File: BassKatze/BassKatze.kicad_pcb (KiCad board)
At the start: 2 copper layers, 55 x 54.9 mm, 54 parts, among them J1 Conn_01x02_Female, Q1 IRF7404, Q2 BSS138, Q3 BSS138, Q4 BSS138, Q5 BSS138, Q6 BSS138, SW1 SW_Push, U1 ATmega328-AU, U2 MSGEQ7, U3 TP4056

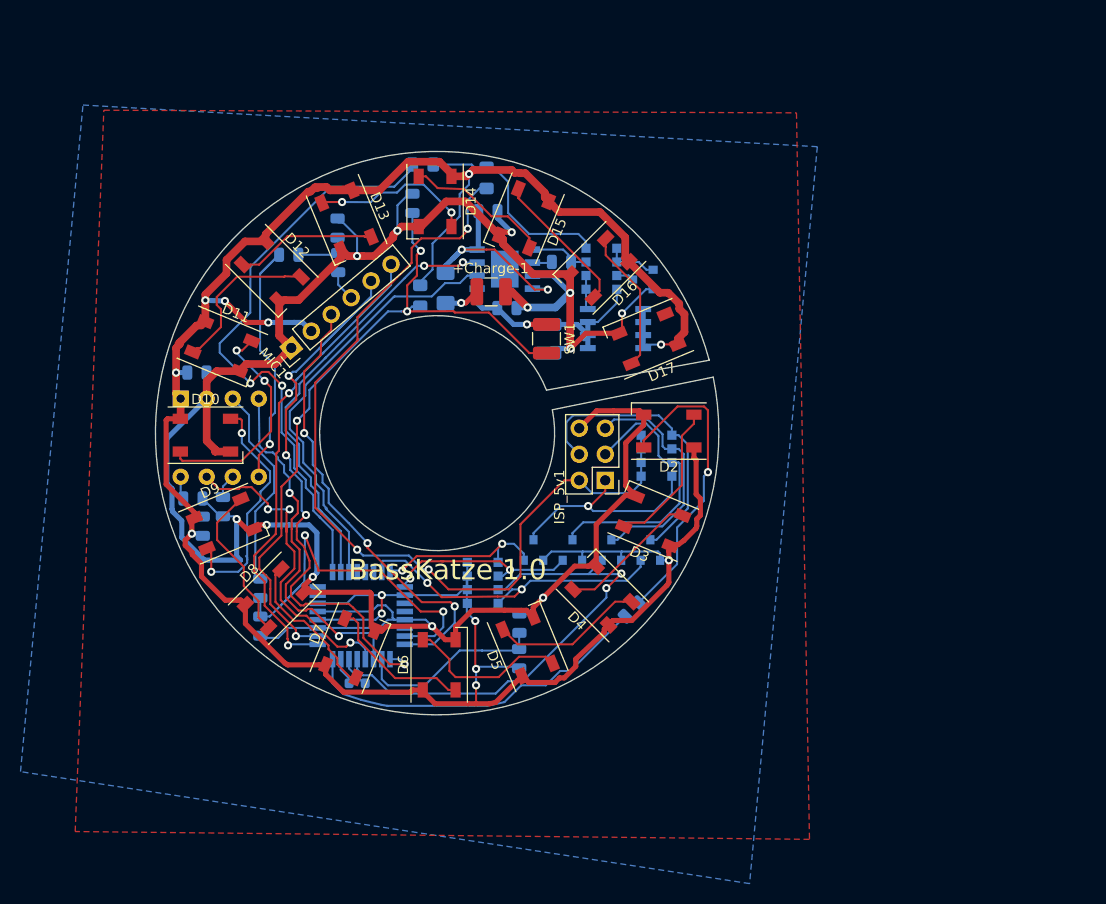
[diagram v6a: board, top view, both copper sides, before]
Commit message: update to esp32 proto
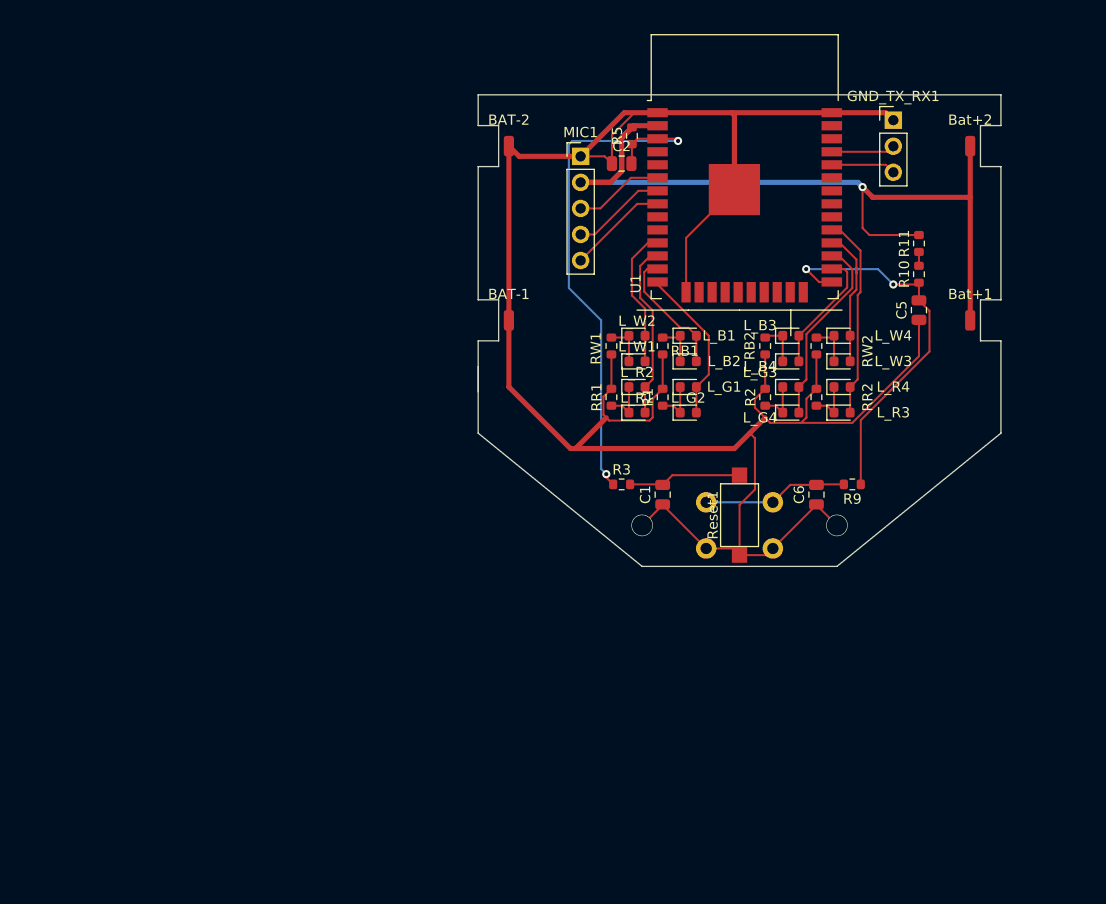
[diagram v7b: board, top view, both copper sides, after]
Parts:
- removed +Bat-1: BAT, Capacitor_SMD:C_1210_3225Metric
- removed +Charge-1: Charge, Capacitor_SMD:C_1210_3225Metric
- removed C3: 0.1uF, Capacitor_SMD:C_0805_2012Metric
- removed C4: 33pF, Capacitor_SMD:C_0805_2012Metric
- removed D1, D18, D19: D, Diode_SMD:D_0805_2012Metric_Pad1.15x1.40mm_HandSolder
- removed D10, D11, D12, D13, D14, D15, D16, D17, D2, D3, D4, D5, D6, D7, D8, D9: SK6812, LED_SMD:LED_SK6812_PLCC4_5.0x5.0mm_P3.2mm
- removed ISP_5v1: Conn_02x03_Counter_Clockwise, Connector_PinHeader_2.54mm:PinHeader_2x03_P2.54mm_Vertical
- removed J1: Conn_01x02_Female, Resistor_SMD:R_0603_1608Metric
- removed Q1: IRF7404, Package_SO:SOIC-8_3.9x4.9mm_P1.27mm
- removed Q2, Q3, Q4, Q5, Q6: BSS138, Package_TO_SOT_SMD:SOT-23
- removed R14: 470Ohm, Resistor_SMD:R_0805_2012Metric
- removed R15: 10k, Resistor_SMD:R_0805_2012Metric
- removed R6: 147KOhm, Resistor_SMD:R_0805_2012Metric
- removed R7: 1KOhm, Resistor_SMD:R_0805_2012Metric
- removed R8: 5KOhm, Resistor_SMD:R_0805_2012Metric
- removed RN1, RN3: R_Pack04, Resistor_SMD:R_Array_Convex_4x1206
- removed RN2: R_Pack0410K, Resistor_SMD:R_Array_Convex_4x1206
- removed RProg1: 1.2kOhm, Resistor_SMD:R_0805_2012Metric
- removed SW1: SW_Push, Capacitor_SMD:C_1210_3225Metric
- removed U2: MSGEQ7, Package_DIP:DIP-8_W7.62mm
- removed U3: TP4056, tp4056:TP4056_SOP-8-PP
- added BAT-1: Conn_01x01_Female, Connector_Wire:SolderWirePad_1x01_SMD_1x2mm, F.Cu at (134.0, 116.0)
- added BAT-2: Conn_01x01_Female, Connector_Wire:SolderWirePad_1x01_SMD_1x2mm, F.Cu at (134.0, 99.0)
- added Bat+1: Conn_01x01_Female, Connector_Wire:SolderWirePad_1x01_SMD_1x2mm, F.Cu at (179.0, 116.0)
- added Bat+2: Conn_01x01_Female, Connector_Wire:SolderWirePad_1x01_SMD_1x2mm, F.Cu at (179.0, 99.0)
- added Boot1: Boot, Button_Switch_THT:SW_PUSH_6mm_H5mm, B.Cu at (153.2, 138.2)
- added GND_TX_RX1: Conn_01x03_Female, Connector_PinHeader_2.54mm:PinHeader_1x03_P2.54mm_Vertical, F.Cu at (171.5, 96.5)
- added L_B1: LED_BLUE, LED_SMD:LED_0603_1608Metric, F.Cu at (151.5, 117.5)
- added L_B2: LED_BLUE, LED_SMD:LED_0603_1608Metric, F.Cu at (151.5, 120.0)
- added L_B3: LED_BLUE, LED_SMD:LED_0603_1608Metric, F.Cu at (161.5, 117.5)
- added L_B4: LED_BLUE, LED_SMD:LED_0603_1608Metric, F.Cu at (161.5, 120.0)
- added L_G1: LED_GREEN, LED_SMD:LED_0603_1608Metric, F.Cu at (151.5, 122.5)
- added L_G2: LED_GREEN, LED_SMD:LED_0603_1608Metric, F.Cu at (151.5, 125.0)
- added L_G3: LED_GREEN, LED_SMD:LED_0603_1608Metric, F.Cu at (161.5, 122.5)
- added L_G4: LED_GREEN, LED_SMD:LED_0603_1608Metric, F.Cu at (161.5, 125.0)
- added L_R1: LED_RED, LED_SMD:LED_0603_1608Metric, F.Cu at (146.5, 125.0)
- added L_R2: LED_RED, LED_SMD:LED_0603_1608Metric, F.Cu at (146.5, 122.5)
- added L_R3: LED_RED, LED_SMD:LED_0603_1608Metric, F.Cu at (166.5, 125.0)
- added L_R4: LED_RED, LED_SMD:LED_0603_1608Metric, F.Cu at (166.5, 122.5)
- added L_W1: LED_WHITE, LED_SMD:LED_0603_1608Metric, F.Cu at (146.5, 120.0)
- added L_W2: LED_WHITE, LED_SMD:LED_0603_1608Metric, F.Cu at (146.5, 117.5)
- added L_W3: LED_WHITE, LED_SMD:LED_0603_1608Metric, F.Cu at (166.5, 120.0)
- added L_W4: LED_WHITE, LED_SMD:LED_0603_1608Metric, F.Cu at (166.5, 117.5)
- added R11: 1k, Resistor_SMD:R_0603_1608Metric, F.Cu at (174.0, 108.5)
- added R5: 10k, Resistor_SMD:R_0603_1608Metric, F.Cu at (146.0, 98.0)
- added RB1: R, Resistor_SMD:R_0603_1608Metric, F.Cu at (149.0, 118.5)
- added RB2: R, Resistor_SMD:R_0603_1608Metric, F.Cu at (159.0, 118.5)
- added RR1: R, Resistor_SMD:R_0603_1608Metric, F.Cu at (144.0, 123.5)
- added RR2: R, Resistor_SMD:R_0603_1608Metric, F.Cu at (164.0, 123.5)
- added RW1: R, Resistor_SMD:R_0603_1608Metric, F.Cu at (144.0, 118.5)
- added RW2: R, Resistor_SMD:R_0603_1608Metric, F.Cu at (164.0, 118.5)
- added Reset1: SW_Push, Button_Switch_SMD:SW_SPST_CK_RS282G05A3, F.Cu at (156.5, 135.0)
- C1: value 10uF -> 100n; moved to F.Cu
- C2: value 10uF -> 22uf; moved to F.Cu
- C5: value 0.1uF -> 22uf; moved to F.Cu
- C6: value 0.1uF -> 100n; moved to F.Cu
- MIC1: value MIC -> Conn_01x05; footprint Connector_PinHeader_2.54mm:PinHeader_1x06_P2.54mm_Vertical -> Connector_PinHeader_2.54mm:PinHeader_1x05_P2.54mm_Vertical
- R1: value 0.2Ohm -> R; footprint Resistor_SMD:R_1206_3216Metric_Pad1.42x1.75mm_HandSolder -> Resistor_SMD:R_0603_1608Metric; moved to F.Cu
- R10: value 5KOhm -> 1k; footprint Resistor_SMD:R_0805_2012Metric -> Resistor_SMD:R_0603_1608Metric; moved to F.Cu
- R2: value 26KOhm -> R; footprint Resistor_SMD:R_0805_2012Metric -> Resistor_SMD:R_0603_1608Metric; moved to F.Cu
- R3: value 200KOhm -> 1k; footprint Resistor_SMD:R_0805_2012Metric -> Resistor_SMD:R_0603_1608Metric; moved to F.Cu
- R9: value 1KOhm -> 1k; footprint Resistor_SMD:R_0805_2012Metric -> Resistor_SMD:R_0603_1608Metric; moved to F.Cu
- U1: value ATmega328-AU -> ESP32-WROOM-32D; footprint Package_QFP:TQFP-32_7x7mm_P0.8mm -> RF_Module:ESP32-WROOM-32; moved to F.Cu
- moved R10 71.2 mm to (174.0, 111.5), turned to 90 degrees
- moved C5 70.7 mm to (174.0, 115.0), turned to 90 degrees
- moved R9 59.4 mm to (167.5, 132.0), turned to 180 degrees
- moved C6 57.9 mm to (164.0, 133.0), turned to 90 degrees
- moved U1 55.3 mm to (157.0, 104.0)
- moved R2 44.9 mm to (159.0, 123.5), turned to 90 degrees
- moved R3 41.1 mm to (145.0, 132.0), turned to 0 degrees
- moved MIC1 33.8 mm to (141.0, 100.0), turned to 0 degrees
- moved C1 32.5 mm to (149.0, 133.0), turned to 90 degrees
- moved R1 23.7 mm to (149.0, 123.5)
- moved C2 18.0 mm to (145.0, 100.7)
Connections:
- C1 pad 1: Net-(C1-Pad1) -> GND
- C1 pad 2: BAT- -> Net-(C1-Pad2)
- C2 pad 1: BAT+ -> GND
- C2 pad 2: BAT- -> Net-(C2-Pad2)
- C5 pad 1: PWR -> GND
- C5 pad 2: BAT- -> Net-(C5-Pad2)
- C6 pad 1: Net-(C6-Pad1) -> GND
- C6 pad 2: BAT- -> Net-(Boot1-Pad2)
- MIC1 pad 1: BAT- -> GND
- MIC1 pad 2: PWR -> VCC_ALWAYS
- MIC1 pad 4: Net-(MIC1-Pad4) -> Attack_Select
- MIC1 pad 5: Attack_Select -> MIC
- R1 pad 1: 5V_IN -> Net-(L_G1-Pad1)
- R1 pad 2: Net-(C1-Pad1) -> GND
- R10 pad 1: RAW_Spectrum -> Net-(C5-Pad2)
- R2 pad 1: BAT- -> Net-(L_G3-Pad1)
- R2 pad 2: Net-(C3-Pad2) -> GND
- R3 pad 1: Net-(C4-Pad1) -> Net-(C2-Pad2)
- R3 pad 2: PWR -> Net-(C1-Pad2)
- R9 pad 1: Net-(R10-Pad2) -> Net-(C5-Pad2)
- R9 pad 2: BAT- -> Net-(Boot1-Pad2)
- U1 pad 1: Free1 -> GND
- U1 pad 10: CHRG -> unconnected-(U1-Pad10)
- U1 pad 11: STDBY -> LED_W1
- U1 pad 12: (no net) -> LED_R1
- U1 pad 13: (no net) -> LED_B1
- U1 pad 14: (no net) -> LED_G1
- U1 pad 15: MOSI -> GND
- U1 pad 16: MISO -> unconnected-(U1-Pad16)
- U1 pad 17: SCK -> unconnected-(U1-Pad17)
- U1 pad 18: PWR -> unconnected-(U1-Pad18)
- U1 pad 19: (no net) -> unconnected-(U1-Pad19)
- U1 pad 2: Button -> VCC_ALWAYS
- U1 pad 20: (no net) -> unconnected-(U1-Pad20)
- U1 pad 21: BAT- -> unconnected-(U1-Pad21)
- U1 pad 22: (no net) -> unconnected-(U1-Pad22)
- U1 pad 23: Net-(R10-Pad2) -> STDBY
- U1 pad 24: Gain_Select -> CUSTOM_GPIO2
- U1 pad 25: Attack_Select -> Net-(C5-Pad2)
- U1 pad 26: Net-(R7-Pad1) -> LED_B2
- U1 pad 27: EQ_Band -> LED_G2
- U1 pad 28: EQ_Reset -> LED_W2
- U1 pad 29: Reset -> LED_R2
- U1 pad 3: BAT- -> Net-(C2-Pad2)
- U1 pad 30: Net-(J1-Pad1) -> unconnected-(U1-Pad30)
- U1 pad 31: Net-(J1-Pad2) -> unconnected-(U1-Pad31)
- U1 pad 32: Net-(R14-Pad2) -> unconnected-(U1-Pad32)
- U1 pad 4: PWR -> unconnected-(U1-Pad4)
- U1 pad 5: BAT- -> unconnected-(U1-Pad5)
- U1 pad 6: PWR -> Gain_Select
- U1 pad 7: (no net) -> Attack_Select
- U1 pad 8: (no net) -> MIC
- U1 pad 9: PWR_HOLD -> unconnected-(U1-Pad9)
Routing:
- net PWR: track 277.0 -> 0.00 mm, vias 13 -> 0
- net BAT-: track 267.1 -> 0.00 mm, vias 12 -> 0
- net GND: track 0.00 -> 218.0 mm, vias 0 -> 2
- net 5V_Flash: track 88.9 -> 0.00 mm, vias 3 -> 0
- net VCC_ALWAYS: track 0.00 -> 87.8 mm, vias 0 -> 1
- net Button: track 71.3 -> 0.00 mm, vias 4 -> 0
- net PWR_HOLD: track 58.5 -> 0.00 mm, vias 2 -> 0
- net Net-(C2-Pad2): track 0.00 -> 52.4 mm, vias 0 -> 2
- net Attack_Select: track 61.2 -> 9.26 mm, vias 4 -> 0
- net Reset: track 47.7 -> 0.00 mm, vias 2 -> 0
- net Free1: track 47.6 -> 0.00 mm, vias 2 -> 0
- net CHRG: track 44.0 -> 0.00 mm, vias 2 -> 0
- net STDBY: track 42.6 -> 0.00 mm
- net Net-(C5-Pad2): track 0.00 -> 37.6 mm, vias 0 -> 2
- net Net-(R10-Pad2): track 38.8 -> 1.35 mm, vias 2 -> 0
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- removed copper zone on B.Cu, net BAT-
- removed copper zone on F.Cu, net BAT-
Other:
- board size 55 x 54.9 mm -> 51 x 46 mm
- net class Default removed
- net class High removed
- board text removed: "BassKatze 1.0"

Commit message: esp32 version
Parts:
- added C1: 100n, Capacitor_SMD:C_0805_2012Metric, F.Cu at (149.0, 133.0)
- added C3: 100nF, Capacitor_SMD:C_0603_1608Metric, F.Cu at (136.8, 117.2)
- added JP1: Jumper_2_Bridged, Jumper:SolderJumper-2_P1.3mm_Bridged_RoundedPad1.0x1.5mm, F.Cu at (138.2, 125.8)
- added Q1: N-channel 30V 5A, Package_TO_SOT_SMD:SOT-23, F.Cu at (134.8, 121.0)
- added Q2: N-channel 30V 5A, Package_TO_SOT_SMD:SOT-23, F.Cu at (134.8, 125.8)
- added R4: 20k?, Resistor_SMD:R_0603_1608Metric, F.Cu at (141.2, 127.5)
- added R6: 100Ohm, Resistor_SMD:R_0603_1608Metric, F.Cu at (139.5, 116.8)
- added U2: hy2112, Package_TO_SOT_SMD:SOT-23-6_Handsoldering, F.Cu at (140.0, 121.0)
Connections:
- net VCC_ALWAYS renamed 3V3
- BAT-1 pad 1: GND -> BAT-
- BAT-2 pad 1: GND -> BAT-
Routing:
- net GND: track 218.0 -> 259.6 mm, vias 2 -> 23
- net BAT-: track 0.00 -> 25.9 mm
- net Net-(Q2-Pad1): track 0.00 -> 16.8 mm
- net 3V3: track 87.8 -> 101.8 mm
- net Net-(JP1-Pad1): track 0.00 -> 13.3 mm
- net Net-(R4-Pad1): track 0.00 -> 4.84 mm
- net Net-(C3-Pad1): track 0.00 -> 4.39 mm
- net Net-(Q1-Pad1): track 0.00 -> 3.53 mm
- added copper zone on B.Cu, net GND
- added copper zone on F.Cu, net GND
